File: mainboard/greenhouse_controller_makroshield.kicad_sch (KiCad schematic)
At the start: 44 parts

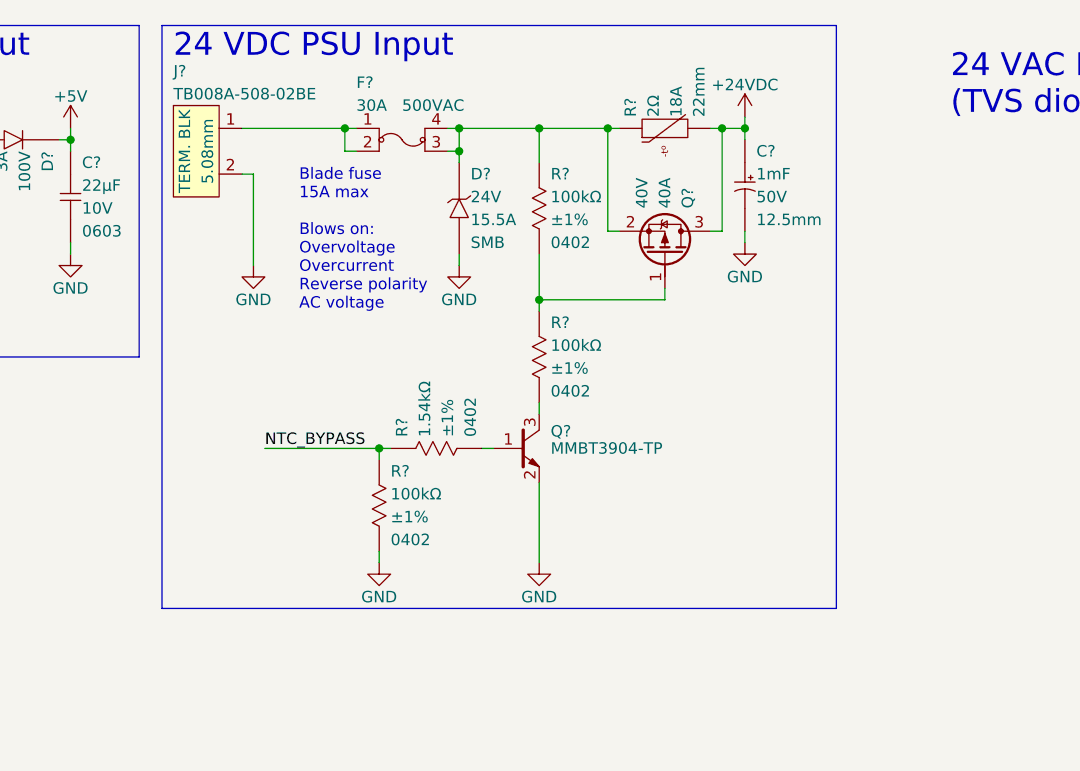
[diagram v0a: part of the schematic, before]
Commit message: Split project in two parts: mainboard and motor driver boards
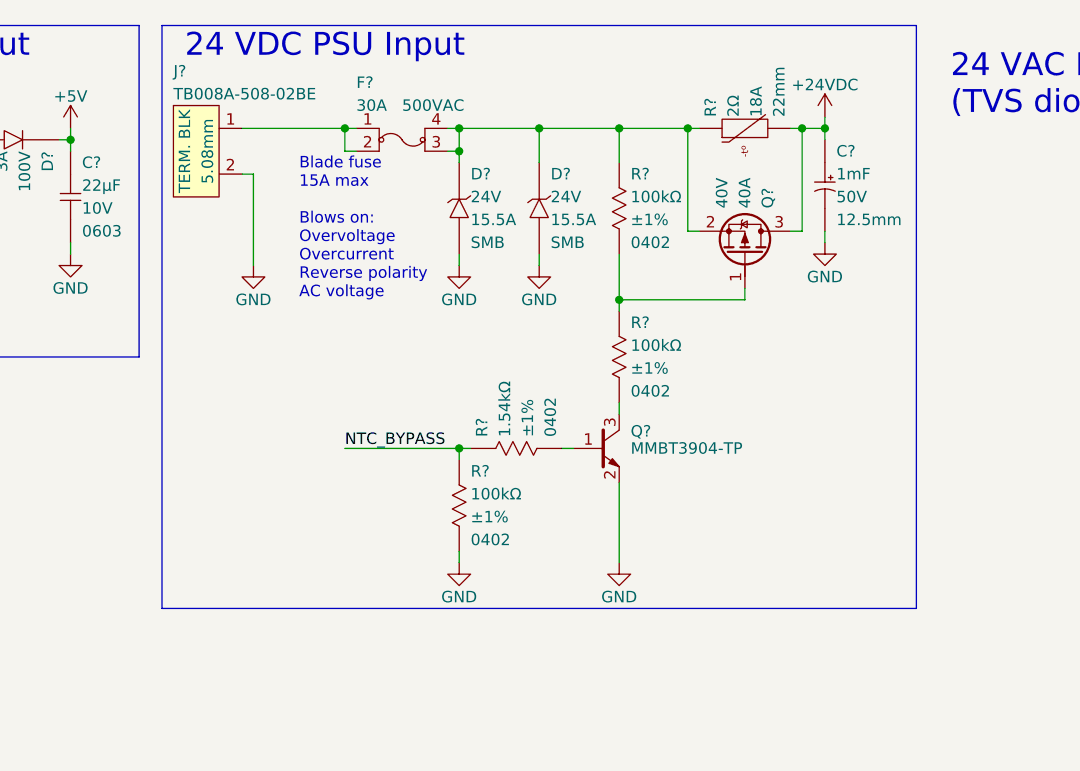
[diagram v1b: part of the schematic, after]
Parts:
- added D?: DIO_TVS_24V_UNI_SMB, connaxio-diodes:DO-124AA_SMB, symbol connaxio-diodes:DIO_TVS_24V_UNI_SMB
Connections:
- net GND: now also D?.2 (A)
- net at D?.1 (K), F?.3, F?.4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: now also D?.1 (K)
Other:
- moved on the sheet: C?, D?, Q?, R?

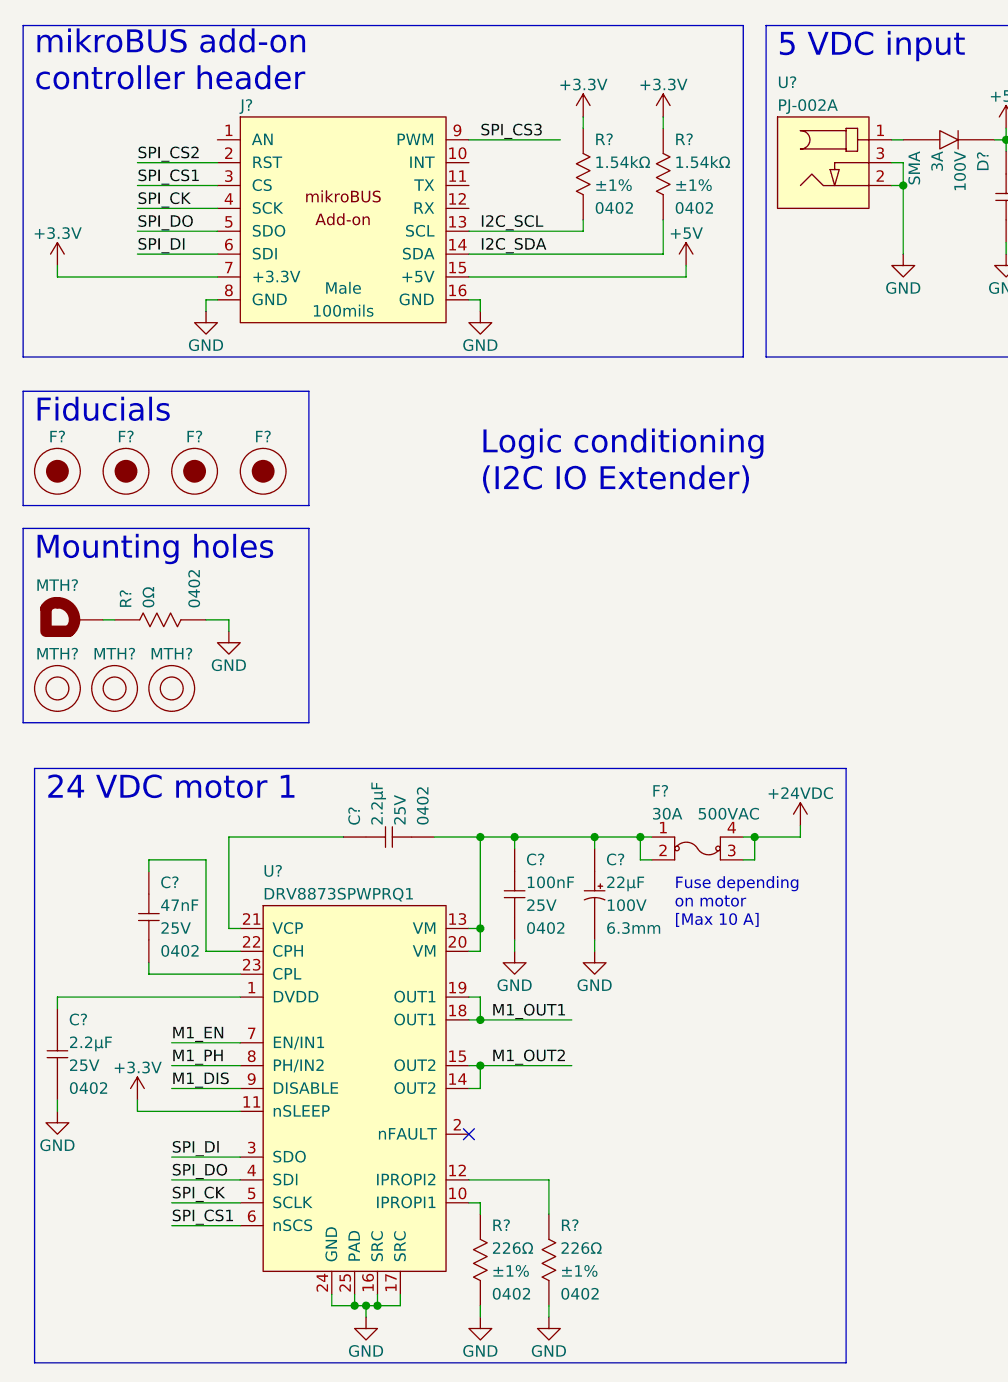
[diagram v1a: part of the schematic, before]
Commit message: Complete H bridge driver
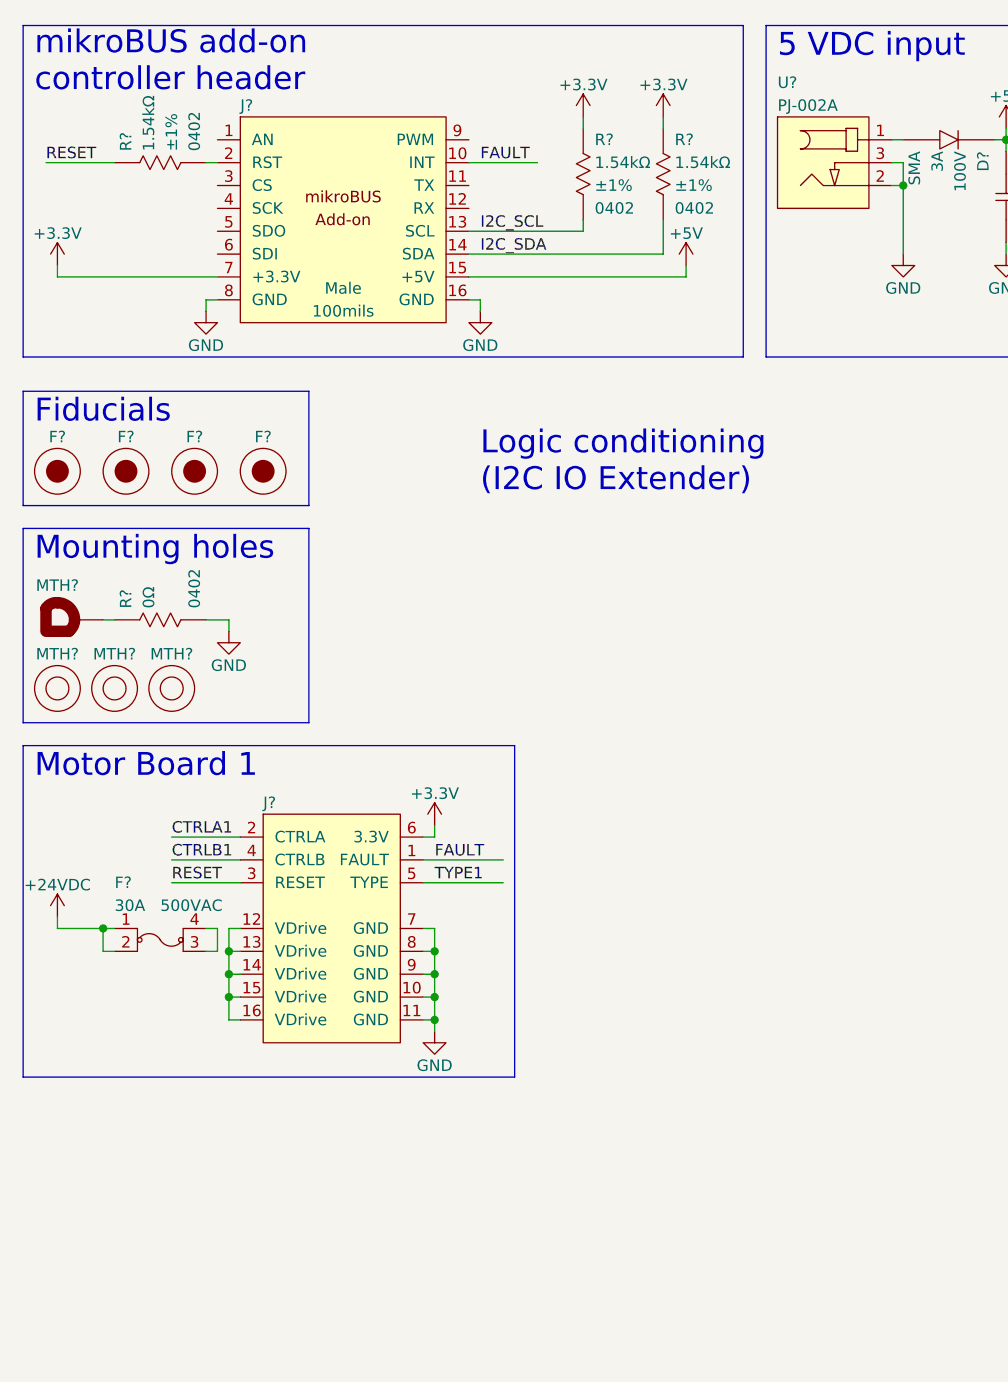
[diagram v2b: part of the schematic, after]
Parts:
- removed C? (x2): CAP_CER_2.2UF_25V_0402, connaxio-capacitors:CAP_CER_0402_1005M, symbol connaxio-capacitors:CAP_CER_2.2UF_25V_0402
- removed C?: CAP_AE_22UF_100V_TH_6.3MM, connaxio-capacitors:CAP_AE_RAD_D6.3_H12.5_P2.5, symbol connaxio-capacitors:CAP_AE_22UF_100V_TH_6.3MM
- removed C?: CAP_CER_100NF_25V_0402, connaxio-capacitors:CAP_CER_0402_1005M, symbol connaxio-capacitors:CAP_CER_100NF_25V_0402
- removed C?: CAP_CER_47NF_25V_0402, connaxio-capacitors:CAP_CER_0402_1005M, symbol connaxio-capacitors:CAP_CER_47NF_25V_0402
- removed F?: FUS_BLADE_3522, connaxio-connectors:FUS_BLADE_3522, symbol connaxio-connectors:FUS_BLADE_3522
- removed R? (x2): RES_226Ω_1%_0402, connaxio-resistors:RES_0402_1005M, symbol connaxio-resistors:RES_226Ω_1%_0402
- removed U?: DRV_DRV8873SPWPRQ1, connaxio-sop:TSSOP-24_4.4x7.8_P0.65_EP3.2x5.26, symbol connaxio-ic:DRV_DRV8873SPWPRQ1
- added F?: FUS_BLADE_3522, connaxio-connectors:FUS_BLADE_3522, symbol connaxio-connectors:FUS_BLADE_3522
- added J?: CON_CONNAXIO_MOTOR_DRIVER, connaxio-connectors:CON_HDR_100MILS_F_TH_2X8, symbol connaxio-connectors:CON_CONNAXIO_MOTOR_DRIVER
- added R?: RES_1.54KΩ_1%_0402, connaxio-resistors:RES_0402_1005M, symbol connaxio-resistors:RES_1.54KΩ_1%_0402
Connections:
- net +24VDC: now also F?.1, F?.2
- net +3.3V: now also J?.6 (3.3V)
- net GND: now also J?.10 (GND), J?.11 (GND), J?.7 (GND), J?.8 (GND), J?.9 (GND)
- net FAULT: now reaches J?.10 (INT)
- net FAULT: now also J?.1 (FAULT)
- net SPI_CK: no longer names the net of J?.4 (SCK)
- net SPI_CS1: no longer names the net of J?.3 (CS)
- net SPI_CS2: no longer names the net of J?.2 (RST)
- net SPI_CS2: now also R?.2
- net SPI_CS3: no longer names the net of J?.9 (PWM)
- net SPI_DI: no longer names the net of J?.6 (SDI)
- net SPI_DO: no longer names the net of J?.5 (SDO)
- new net: F?.3, F?.4
- new net: J?.12 (VDrive), J?.13 (VDrive), J?.14 (VDrive), J?.15 (VDrive), J?.16 (VDrive)
- new net CTRLA1: J?.2 (CTRLA)
- new net CTRLB1: J?.4 (CTRLB)
- new net RESET: J?.3 (RESET), R?.1
- new net TYPE1: J?.5 (TYPE)
- no-connect marks 1 -> 0
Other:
- note added: "Motor Board 1"
- note removed: "24 VDC motor 1"
- note removed: "Fuse depending on motor [Max 10 A]"
